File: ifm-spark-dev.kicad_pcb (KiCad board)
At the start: 2 copper layers, 23.4 x 24.6 mm, 25 parts, among them J1 CONN_01X03_MALE, J2 CONN_01X06, J3 CONN_01X02, J4 CONN_01X07, J5 CONN_01X03_MALE, SW1 PTS525-SM15, U1 STM32F030x4, Y1 8MHz

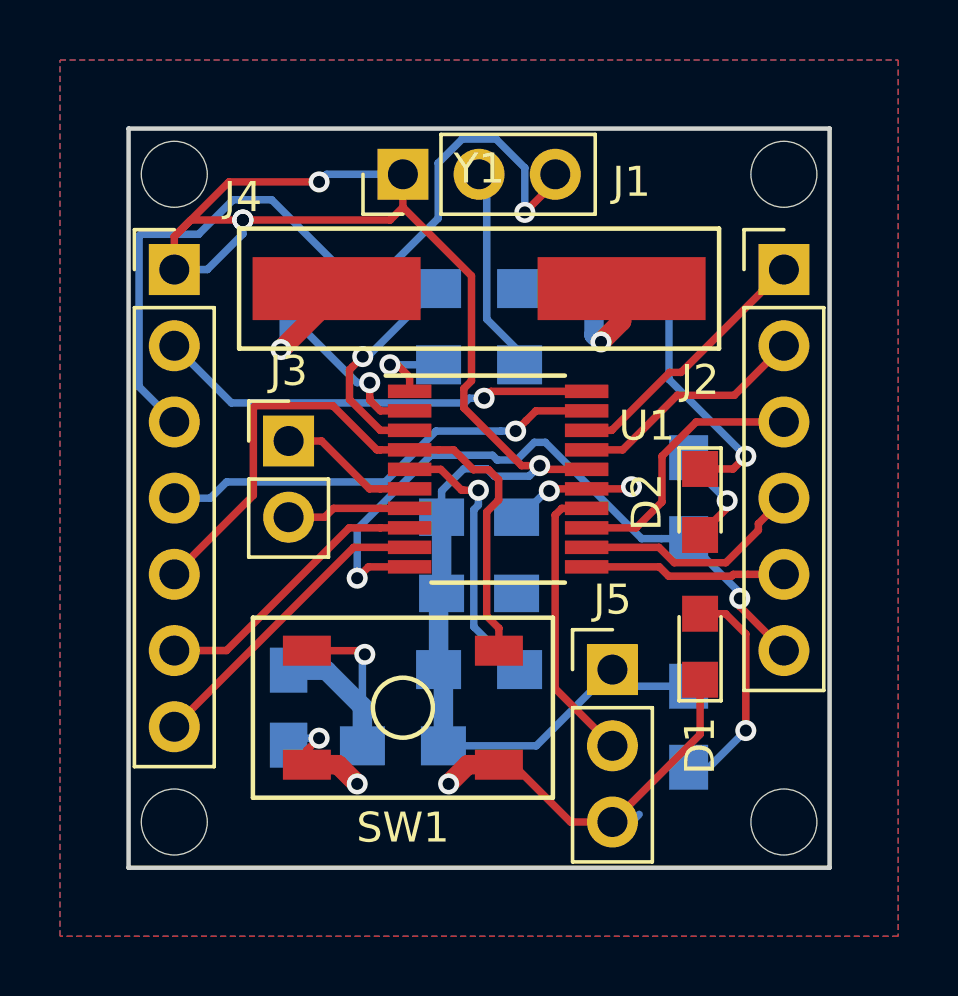
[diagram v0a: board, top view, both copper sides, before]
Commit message: Added some labels and identifiers and cleaned up some tracks
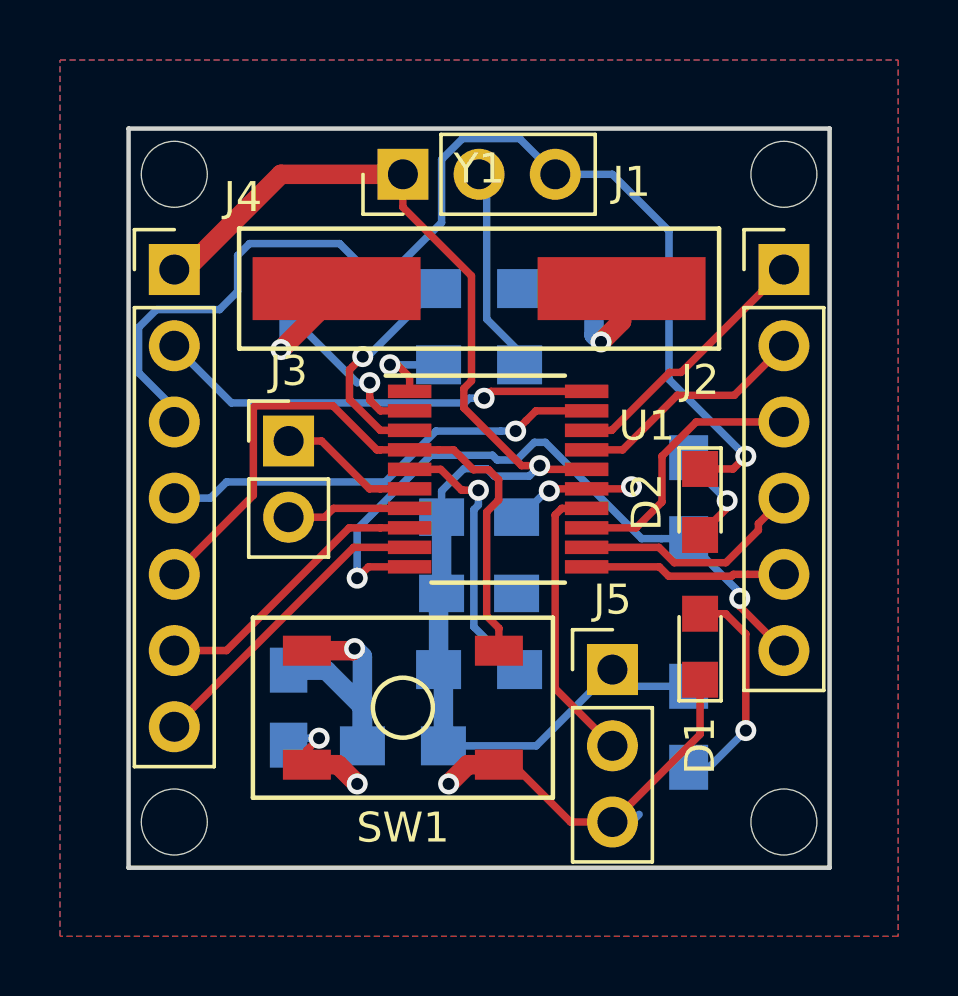
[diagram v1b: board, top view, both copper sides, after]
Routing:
- net +3V3: track 56.5 -> 44.6 mm, vias 4 -> 1
- net GND: track 58.2 -> 61.1 mm, vias 7 -> 6
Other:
- board text added: "1" Challenge"
- board text added: "Cortex-M0"
- board text added: "IFM-Spark Dev"
- board text added: "Rev A"
- board text added: "Stephen Legge"
- board text added: "[ A Legge Up ]"
